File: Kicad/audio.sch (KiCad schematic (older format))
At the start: 70 parts, among them J201 CD Audio In, J202 AC'97 Audio Header, J203 Line Out, U201 TLV320AIC23BPW, U202 STX-4335-5BGP-S1, Y201 12M 20pF

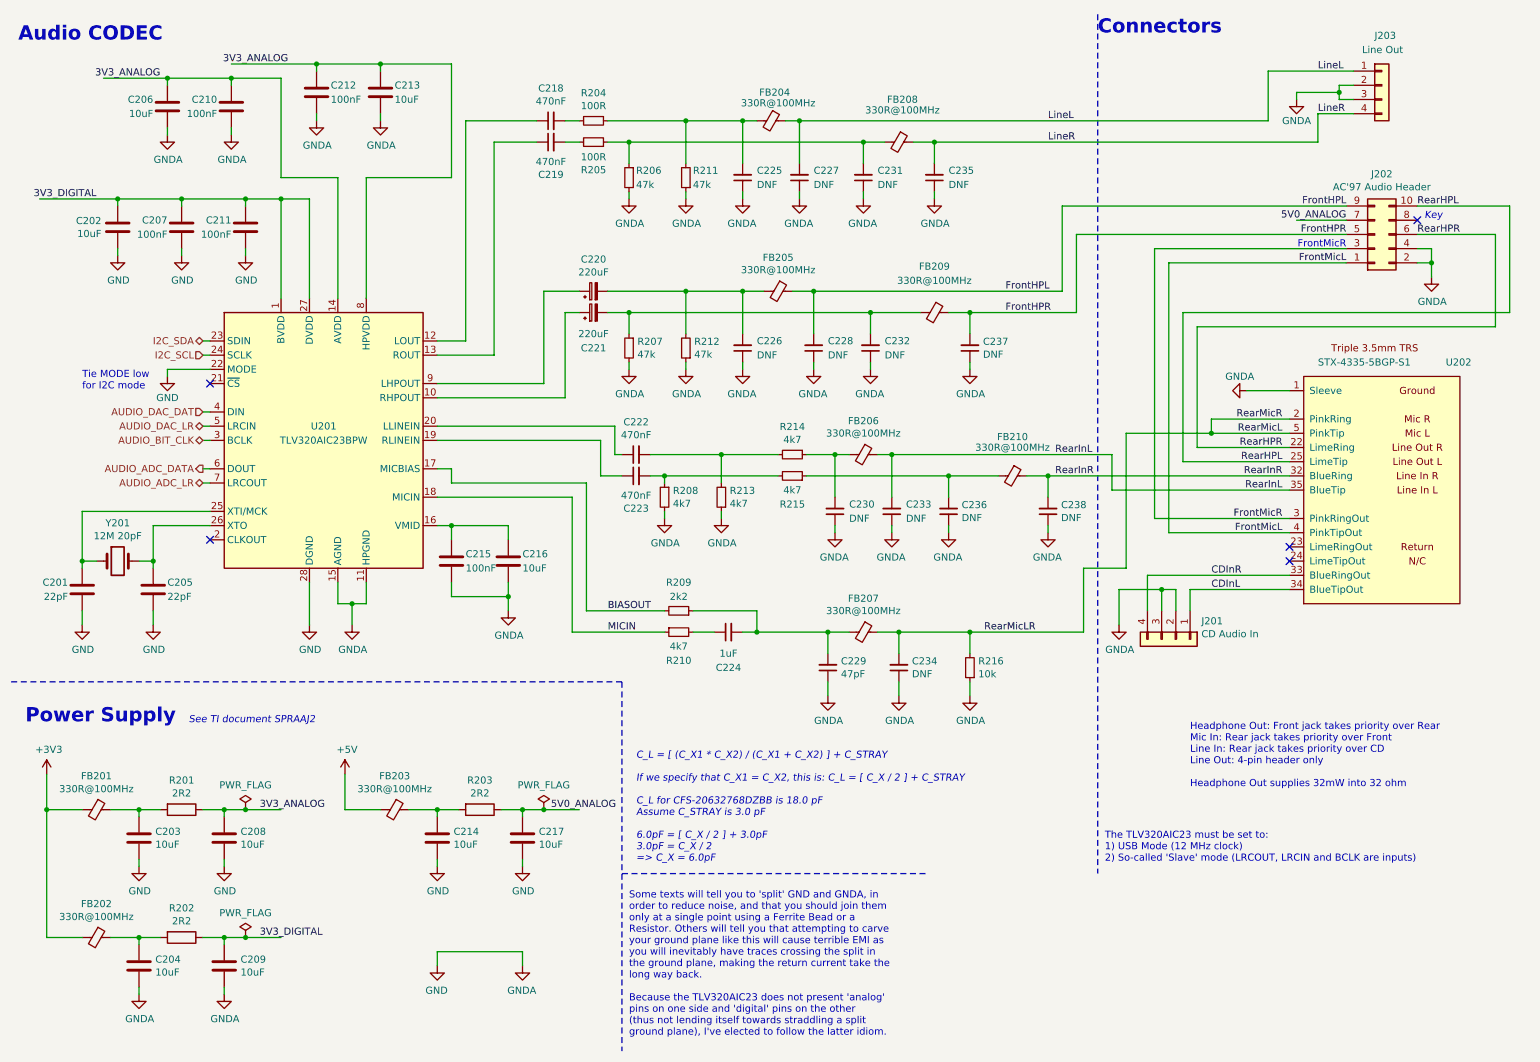
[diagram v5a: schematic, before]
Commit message: Update component values.
Tolerance and Voltage are set to the minimum acceptable. The selected
parts can be better, where a better part is cheaper or has
better availability.

Also dropped R2R DAC tolerance to 1% - 0.5% was overkill. The output
resistor had the wrong value too, which is fixed.
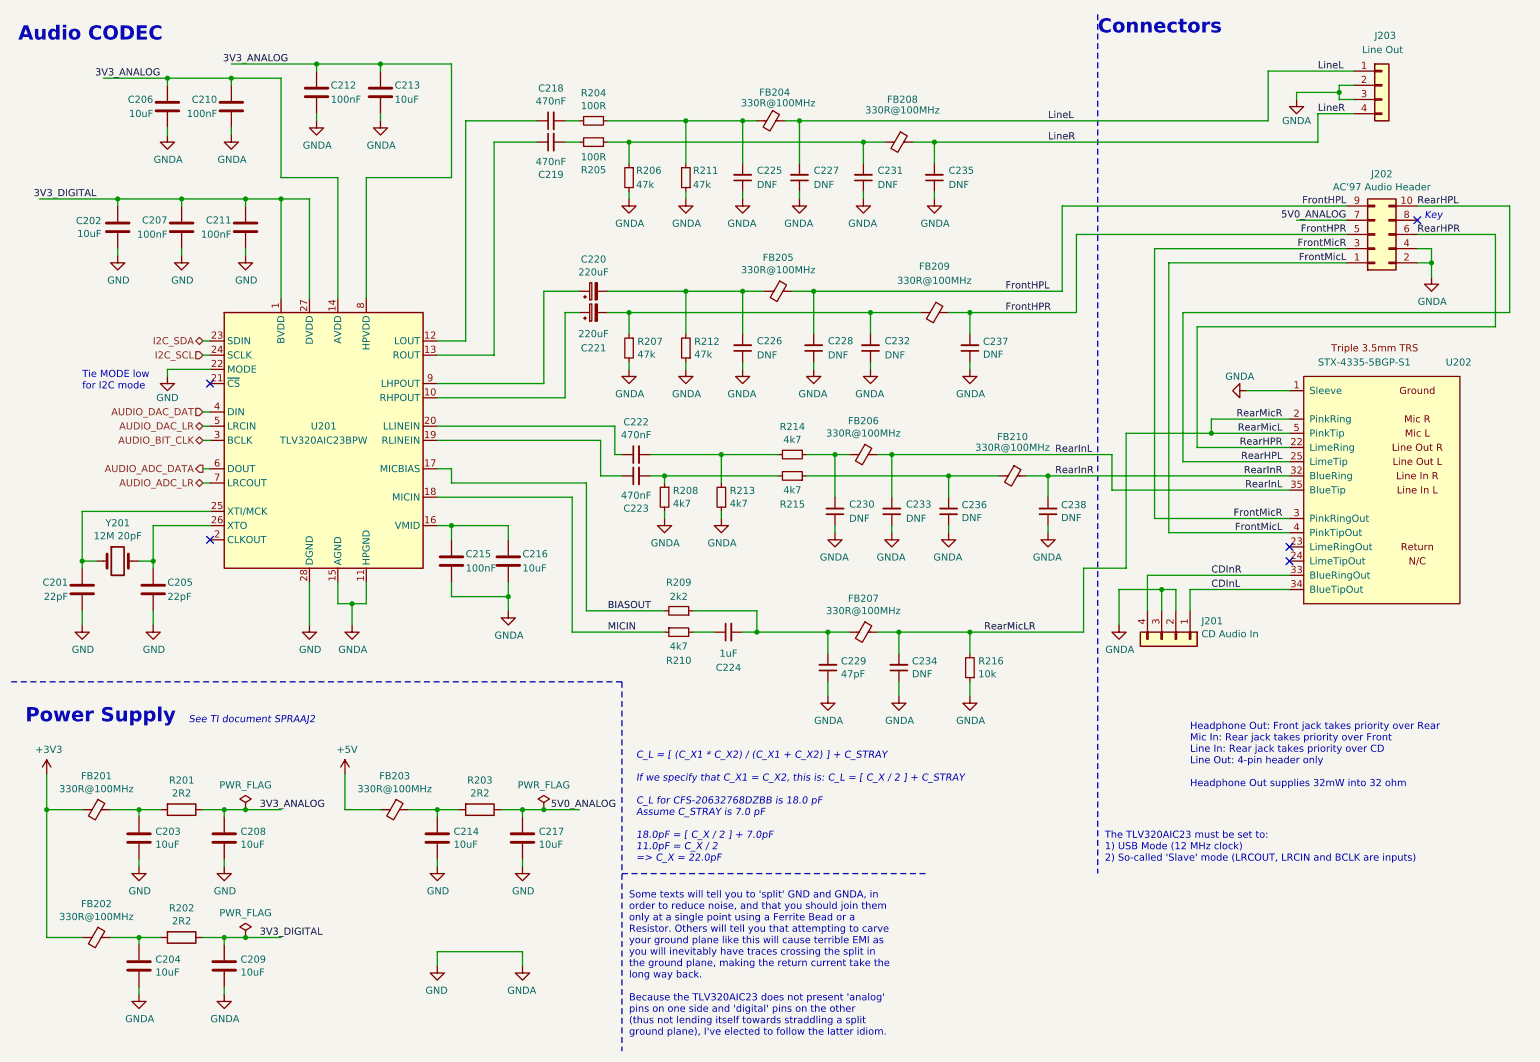
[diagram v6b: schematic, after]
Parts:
- C201, C205: Tolerance (none) -> C0G; Voltage C0G -> 50V
- C202, C203, C204, C206, C208, C209, C213, C214, C216, C217: Tolerance (none) -> X5R; Voltage (none) -> 16V
- C207, C210, C211, C212, C215: Tolerance (none) -> X5R; Voltage (none) -> 50V
- C218, C219, C222, C223: MPN FG18X7R1H474KRT06 -> CL21B474KBFNNNE; Tolerance (none) -> X5R; Voltage (none) -> 50V
- C220, C221: Tolerance (none) -> 20%; Voltage (none) -> 50V
- C224: Tolerance (none) -> X5R; Voltage (none) -> 25V
- C229: Tolerance (none) -> C0G; Voltage (none) -> 50V
- FB201, FB202, FB203, FB204, FB205, FB206, FB207, FB208, FB209, FB210: Tolerance (none) -> 1.5A
- R201, R202, R203, R204, R205, R206, R207, R208, R209, R210, R211, R212, R213, R214, R215, R216: Tolerance (none) -> 1%
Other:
- note added: "C_L = [ (C_X1 * C_X2) / (C_X1 + C_X2) ] + C_STRAY\n\nIf we specify that C_X1 = C_X2, this is: C_L = [ C_X / 2 ] + C_STRAY\n\nC_L for CFS-20632768DZBB is 18.0 pF\nAssume C_STRAY is 7.0 pF \n\n18.0pF = [ C_X / 2 ] + 7.0pF\n11.0pF = C_X / 2\n=> C_X = 22.0pF"
- note removed: "C_L = [ (C_X1 * C_X2) / (C_X1 + C_X2) ] + C_STRAY\n\nIf we specify that C_X1 = C_X2, this is: C_L = [ C_X / 2 ] + C_STRAY\n\nC_L for CFS-20632768DZBB is 18.0 pF\nAssume C_STRAY is 3.0 pF \n\n6.0pF = [ C_X / 2 ] + 3.0pF\n3.0pF = C_X / 2\n=> C_X = 6.0pF"
- note removed: "FrontMicR"

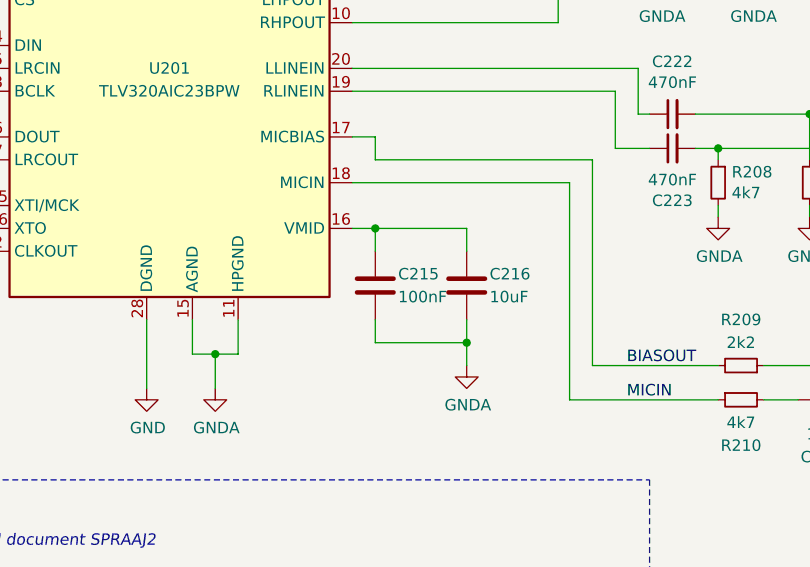
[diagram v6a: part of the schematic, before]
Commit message: Drop capacitor voltage ratings where possible.
Audio circuit is 1V RMS, so 6.3V is fine.
Use 10V for 3.3V circuits.
Use 16V for 5.0V circuits.
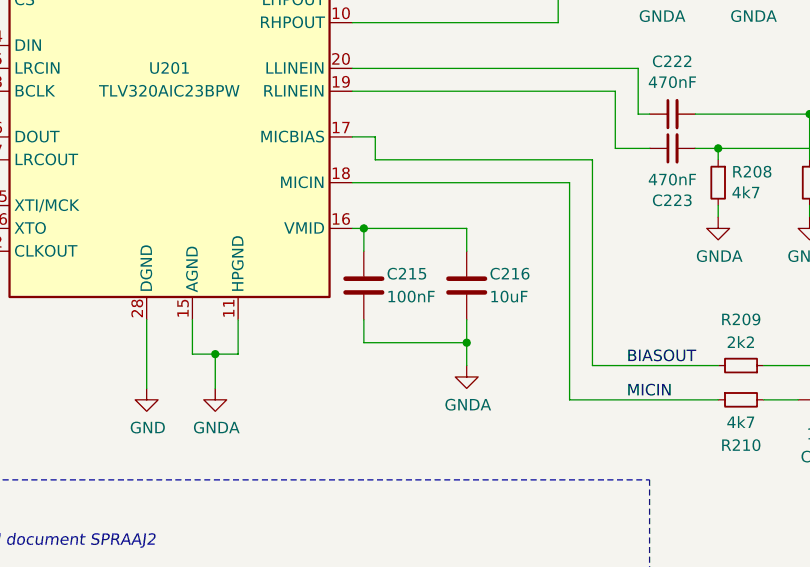
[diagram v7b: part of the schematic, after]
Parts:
- C201, C205: Voltage 50V -> 16V
- C202, C203, C204, C206, C208, C209, C213, C216: Voltage 16V -> 10V
- C207, C210, C211, C212, C215: Voltage 50V -> 10V
- C218, C219, C220, C221, C222, C223, C229: Voltage 50V -> 6.3V
- C224: Voltage 25V -> 6.3V
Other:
- moved on the sheet: C215
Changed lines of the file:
@@
 F 8 "C15850" H 4000 4350 50  0001 C CNN "LCSC Part#"
 F 9 "X5R" H 4000 4350 50  0001 C CNN "Tolerance"
-F 10 "16V" H 4000 4350 50  0001 C CNN "Voltage"
+F 10 "10V" H 4000 4350 50  0001 C CNN "Voltage"
 F 11 "~" H 4000 4350 50  0001 C CNN "Mouser"
 	1    4000 4350
@@
 L Device:C C215
 U 1 1 5FE524BE
-P 3600 4350
-F 0 "C215" H 3700 4400 50  0000 L CNN
-F 1 "100nF" H 3700 4300 50  0000 L CNN
-F 2 "Capacitor_SMD:C_0805_2012Metric_Pad1.18x1.45mm_HandSolder" H 3638 4200 50  0001 C CNN
-F 3 "~" H 3600 4350 50  0001 C CNN
-F 4 "0" H 3600 4350 50  0001 C CNN "DNP"
-F 5 "~" H 3600 4350 50  0001 C CNN "Digikey"
-F 6 "CPL" H 3600 4350 50  0001 C CNN "Manufacturer"
-F 7 "CPL-CAP-X7R-0805-100NF-50V" H 3600 4350 50  0001 C CNN "MPN"
-F 8 "~" H 3600 4350 50  0001 C CNN "Mouser"
-F 9 "C49678" H 3600 4350 50  0001 C CNN "LCSC Part#"
-F 10 "X5R" H 3600 4350 50  0001 C CNN "Tolerance"
-F 11 "50V" H 3600 4350 50  0001 C CNN "Voltage"
-	1    3600 4350
+P 3550 4350
+F 0 "C215" H 3650 4400 50  0000 L CNN
+F 1 "100nF" H 3650 4300 50  0000 L CNN
+F 2 "Capacitor_SMD:C_0805_2012Metric_Pad1.18x1.45mm_HandSolder" H 3588 4200 50  0001 C CNN
+F 3 "~" H 3550 4350 50  0001 C CNN
+F 4 "0" H 3550 4350 50  0001 C CNN "DNP"
+F 5 "~" H 3550 4350 50  0001 C CNN "Digikey"
+F 6 "CPL" H 3550 4350 50  0001 C CNN "Manufacturer"
+F 7 "CPL-CAP-X7R-0805-100NF-50V" H 3550 4350 50  0001 C CNN "MPN"
+F 8 "~" H 3550 4350 50  0001 C CNN "Mouser"
+F 9 "C49678" H 3550 4350 50  0001 C CNN "LCSC Part#"
+F 10 "X5R" H 3550 4350 50  0001 C CNN "Tolerance"
+F 11 "10V" H 3550 4350 50  0001 C CNN "Voltage"
+	1    3550 4350
 	1    0    0    -1
 $EndComp
@@
 	4000 4700 4000 4600
 Wire Wire Line
-	4000 4600 3600 4600
-Wire Wire Line
-	3600 4600 3600 4500
-Wire Wire Line
-	3600 4100 3500 4100
-Wire Wire Line
-	3600 4100 4000 4100
+	4000 4600 3550 4600
+Wire Wire Line
+	3550 4600 3550 4500
+Wire Wire Line
+	3550 4100 3500 4100
+Wire Wire Line
+	3550 4100 4000 4100
 Wire Wire Line
 	4000 4500 4000 4600
-Connection ~ 3600 4100
+Connection ~ 3550 4100
 Connection ~ 4000 4600
 $Comp
@@
 F 7 "Samsung" H 1000 4550 50  0001 C CNN "Manufacturer"
 F 8 "C1804" H 1000 4550 50  0001 C CNN "LCSC Part#"
-F 9 "50V" H 1000 4550 50  0001 C CNN "Voltage"
+F 9 "16V" H 1000 4550 50  0001 C CNN "Voltage"
 F 10 "C0G" H 1000 4550 50  0001 C CNN "Tolerance"
 F 11 "~" H 1000 4550 50  0001 C CNN "Mouser"
@@
 F 7 "Samsung" H 1500 4550 50  0001 C CNN "Manufacturer"
 F 8 "C1804" H 1500 4550 50  0001 C CNN "LCSC Part#"
-F 9 "50V" H 1500 4550 50  0001 C CNN "Voltage"
+F 9 "16V" H 1500 4550 50  0001 C CNN "Voltage"
 F 10 "C0G" H 1500 4550 50  0001 C CNN "Tolerance"
 F 11 "~" H 1500 4550 50  0001 C CNN "Mouser"
@@
 F 8 "C15850" H 1600 1150 50  0001 C CNN "LCSC Part#"
 F 9 "X5R" H 1600 1150 50  0001 C CNN "Tolerance"
-F 10 "16V" H 1600 1150 50  0001 C CNN "Voltage"
+F 10 "10V" H 1600 1150 50  0001 C CNN "Voltage"
 F 11 "~" H 1600 1150 50  0001 C CNN "Mouser"
 	1    1600 1150
@@
 F 9 "C49678" H 2050 1150 50  0001 C CNN "LCSC Part#"
 F 10 "X5R" H 2050 1150 50  0001 C CNN "Tolerance"
-F 11 "50V" H 2050 1150 50  0001 C CNN "Voltage"
+F 11 "10V" H 2050 1150 50  0001 C CNN "Voltage"
 	1    2050 1150
 	-1   0    0    -1
@@
 F 8 "C15850" H 3100 1050 50  0001 C CNN "LCSC Part#"
 F 9 "X5R" H 3100 1050 50  0001 C CNN "Tolerance"
-F 10 "16V" H 3100 1050 50  0001 C CNN "Voltage"
+F 10 "10V" H 3100 1050 50  0001 C CNN "Voltage"
 F 11 "~" H 3100 1050 50  0001 C CNN "Mouser"
 	1    3100 1050
@@
 F 9 "C49678" H 2650 1050 50  0001 C CNN "LCSC Part#"
 F 10 "X5R" H 2650 1050 50  0001 C CNN "Tolerance"
-F 11 "50V" H 2650 1050 50  0001 C CNN "Voltage"
+F 11 "10V" H 2650 1050 50  0001 C CNN "Voltage"
 	1    2650 1050
 	1    0    0    -1
@@
 F 9 "C49678" H 1700 2000 50  0001 C CNN "LCSC Part#"
 F 10 "X5R" H 1700 2000 50  0001 C CNN "Tolerance"
-F 11 "50V" H 1700 2000 50  0001 C CNN "Voltage"
+F 11 "10V" H 1700 2000 50  0001 C CNN "Voltage"
 	1    1700 2000
 	-1   0    0    -1
@@
 F 9 "C49678" H 2150 2000 50  0001 C CNN "LCSC Part#"
 F 10 "X5R" H 2150 2000 50  0001 C CNN "Tolerance"
-F 11 "50V" H 2150 2000 50  0001 C CNN "Voltage"
+F 11 "10V" H 2150 2000 50  0001 C CNN "Voltage"
 	1    2150 2000
 	-1   0    0    -1
@@
 F 9 "C13967" H 4300 1400 50  0001 C CNN "LCSC Part#"
 F 10 "X5R" H 4300 1400 50  0001 C CNN "Tolerance"
-F 11 "50V" H 4300 1400 50  0001 C CNN "Voltage"
+F 11 "6.3V" H 4300 1400 50  0001 C CNN "Voltage"
 	1    4300 1400
 	0    -1   -1   0
@@
 F 9 "C13967" H 4300 1250 50  0001 C CNN "LCSC Part#"
 F 10 "X5R" H 4300 1250 50  0001 C CNN "Tolerance"
-F 11 "50V" H 4300 1250 50  0001 C CNN "Voltage"
+F 11 "6.3V" H 4300 1250 50  0001 C CNN "Voltage"
 	1    4300 1250
 	0    -1   1    0
@@
 F 9 "~" H 4600 2450 50  0001 C CNN "LCSC Part#"
 F 10 "20%" H 4600 2450 50  0001 C CNN "Tolerance"
-F 11 "50V" H 4600 2450 50  0001 C CNN "Voltage"
+F 11 "6.3V" H 4600 2450 50  0001 C CNN "Voltage"
 	1    4600 2450
 	0    -1   -1   0
@@
 F 9 "~" H 4600 2600 50  0001 C CNN "LCSC Part#"
 F 10 "20%" H 4600 2600 50  0001 C CNN "Tolerance"
-F 11 "50V" H 4600 2600 50  0001 C CNN "Voltage"
+F 11 "6.3V" H 4600 2600 50  0001 C CNN "Voltage"
 	1    4600 2600
 	0    -1   -1   0
@@
 F 8 "C15850" H 2000 7200 50  0001 C CNN "LCSC Part#"
 F 9 "X5R" H 2000 7200 50  0001 C CNN "Tolerance"
-F 10 "16V" H 2000 7200 50  0001 C CNN "Voltage"
+F 10 "10V" H 2000 7200 50  0001 C CNN "Voltage"
 F 11 "~" H 2000 7200 50  0001 C CNN "Mouser"
 	1    2000 7200
@@
 F 8 "C15850" H 1400 6300 50  0001 C CNN "LCSC Part#"
 F 9 "X5R" H 1400 6300 50  0001 C CNN "Tolerance"
-F 10 "16V" H 1400 6300 50  0001 C CNN "Voltage"
+F 10 "10V" H 1400 6300 50  0001 C CNN "Voltage"
 F 11 "~" H 1400 6300 50  0001 C CNN "Mouser"
 	1    1400 6300
@@
 F 8 "C15850" H 1400 7200 50  0001 C CNN "LCSC Part#"
 F 9 "X5R" H 1400 7200 50  0001 C CNN "Tolerance"
-F 10 "16V" H 1400 7200 50  0001 C CNN "Voltage"
+F 10 "10V" H 1400 7200 50  0001 C CNN "Voltage"
 F 11 "~" H 1400 7200 50  0001 C CNN "Mouser"
 	1    1400 7200
@@
 F 8 "C15850" H 2000 6300 50  0001 C CNN "LCSC Part#"
 F 9 "X5R" H 2000 6300 50  0001 C CNN "Tolerance"
-F 10 "16V" H 2000 6300 50  0001 C CNN "Voltage"
+F 10 "10V" H 2000 6300 50  0001 C CNN "Voltage"
 F 11 "~" H 2000 6300 50  0001 C CNN "Mouser"
 	1    2000 6300
@@
 F 8 "C28323" H 5550 4850 50  0001 C CNN "LCSC Part#"
 F 9 "X5R" H 5550 4850 50  0001 C CNN "Tolerance"
-F 10 "25V" H 5550 4850 50  0001 C CNN "Voltage"
+F 10 "6.3V" H 5550 4850 50  0001 C CNN "Voltage"
 F 11 "~" H 5550 4850 50  0001 C CNN "Mouser"
 	1    5550 4850
@@
 F 8 "C14857" H 6250 5100 50  0001 C CNN "LCSC Part#"
 F 9 "C0G" H 6250 5100 50  0001 C CNN "Tolerance"
-F 10 "50V" H 6250 5100 50  0001 C CNN "Voltage"
+F 10 "6.3V" H 6250 5100 50  0001 C CNN "Voltage"
 F 11 "~" H 6250 5100 50  0001 C CNN "Mouser"
 	1    6250 5100
@@
 Connection ~ 6750 4850
 Wire Wire Line
-	3600 4100 3600 4200
+	3550 4100 3550 4200
 Wire Wire Line
 	4000 4100 4000 4200
@@
 F 9 "C13967" H 4900 3750 50  0001 C CNN "LCSC Part#"
 F 10 "X5R" H 4900 3750 50  0001 C CNN "Tolerance"
-F 11 "50V" H 4900 3750 50  0001 C CNN "Voltage"
+F 11 "6.3V" H 4900 3750 50  0001 C CNN "Voltage"
 	1    4900 3750
 	0    -1   -1   0
@@
 F 9 "C13967" H 4900 3600 50  0001 C CNN "LCSC Part#"
 F 10 "X5R" H 4900 3600 50  0001 C CNN "Tolerance"
-F 11 "50V" H 4900 3600 50  0001 C CNN "Voltage"
+F 11 "6.3V" H 4900 3600 50  0001 C CNN "Voltage"
 	1    4900 3600
 	0    -1   1    0
@@
 F 8 "C15850" H 1250 2000 50  0001 C CNN "LCSC Part#"
 F 9 "X5R" H 1250 2000 50  0001 C CNN "Tolerance"
-F 10 "16V" H 1250 2000 50  0001 C CNN "Voltage"
+F 10 "10V" H 1250 2000 50  0001 C CNN "Voltage"
 F 11 "~" H 1250 2000 50  0001 C CNN "Mouser"
 	1    1250 2000
